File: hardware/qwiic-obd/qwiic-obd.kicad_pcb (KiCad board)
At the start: 4 copper layers, 109.9 x 52.7 mm, 157 parts, among them J101 I2C_STANDARD, J102 DB15_Female_HighDensity, J103 I2C_STANDARD, J401 1x4, J601 PIC-ICSPPOLAR_LOCK, Q201 2N7002, Q202 2N7002, Q203 2N7002, Q301 2N7002, Q501 DMG2301L, Q502 DMG2301L, Q503 MMBT3906, Q504 DMG2301L, Q601 DMG2301L, Q602 2N7002, Q603 2N7002, Q604 2N7002, Q605 2N7002, Q606 2N7002, Q607 2N7002, Q608 2N7002, Q609 2N7002, Q701 2N7002, Q702 2N7002, Q703 2N7002, Q704 MMBT3904, SW401 SW_Push, U201 TS5A3359DCUR, U202 TS5A3359DCUR, U203 TS5A3359DCUR, U204 TS5A3359DCUR, U205 TS5A3359DCUR, U301 TH8056KDC-AAA-008-RE, U302 MCP2557FD-xMF, U401 TCA9534, U402 MCP3423, U403 TCA9534, U404 ADM6320BX33ARJZ-R7, U501 AP63203WU, U502 XC9142B50CMR-G, U601 LM317L_SOT-89, U602 NCS20072, U603 PIC16F15225-I/ST, U701 NCS20072, U702 SC16IS741A, U801 SC18IS602BIPW_128, U802 MCP2515-xST, X701 ASV-12.000MHZ-EJ-T, X801 ASV-12.000MHZ-EJ-T

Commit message: And broke the ground plane again... fixed.
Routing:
- net J1850_BUS-: vias 11 -> 10
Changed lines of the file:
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@@
   (via (at 93.467701 41.651701) (size 0.8) (drill 0.4) (layers "F.Cu" "B.Cu") (net 12))
   (via (at 103.124 26.416) (size 0.8) (drill 0.4) (layers "F.Cu" "B.Cu") (net 12))
-  (via (at 88.9 24.892) (size 0.8) (drill 0.4) (layers "F.Cu" "B.Cu") (net 12))
   (via (at 69.596 42.672) (size 0.8) (drill 0.4) (layers "F.Cu" "B.Cu") (net 12))
   (via (at 81.788 43.688) (size 0.8) (drill 0.4) (layers "F.Cu" "B.Cu") (net 12))
@@
   (segment (start 88.9 24.892) (end 88.9 22.851402) (width 0.2) (layer "In2.Cu") (net 12))
   (segment (start 95.504 24.892) (end 94.996 24.892) (width 0.2) (layer "In2.Cu") (net 12))
+  (segment (start 94.996 24.892) (end 88.9 24.892) (width 0.2) (layer "In2.Cu") (net 12))
   (segment (start 91.952299 41.651701) (end 93.467701 41.651701) (width 0.2) (layer "In2.Cu") (net 12))
   (segment (start 105.156 28.956) (end 100.076 34.036) (width 0.2) (layer "In2.Cu") (net 12))
@@
   (segment (start 62.992 44.0182) (end 62.992 43.688) (width 0.2) (layer "B.Cu") (net 12))
   (segment (start 62.992 44.0182) (end 62.3062 44.0182) (width 0.2) (layer "B.Cu") (net 12))
-  (segment (start 94.996 24.892) (end 88.9 24.892) (width 0.2) (layer "B.Cu") (net 12))
   (segment (start 61.313 43.025) (end 56.870331 43.025) (width 0.2) (layer "B.Cu") (net 12))
   (segment (start 55.768984 49.895) (end 56.870331 49.895) (width 0.25) (layer "F.Cu") (net 13))

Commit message: Like I remember
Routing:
- net J1850_BUS-: track 88.2 -> 87.0 mm
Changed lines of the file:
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@@
   (segment (start 103.124 26.416) (end 97.028 26.416) (width 0.2) (layer "In2.Cu") (net 12))
   (segment (start 91.44 42.164) (end 91.952299 41.651701) (width 0.2) (layer "In2.Cu") (net 12))
-  (segment (start 88.9 24.892) (end 88.9 22.851402) (width 0.2) (layer "In2.Cu") (net 12))
+  (segment (start 90.932 24.892) (end 90.932 24.883402) (width 0.2) (layer "In2.Cu") (net 12))
+  (segment (start 94.996 24.892) (end 90.932 24.892) (width 0.2) (layer "In2.Cu") (net 12))
   (segment (start 95.504 24.892) (end 94.996 24.892) (width 0.2) (layer "In2.Cu") (net 12))
-  (segment (start 94.996 24.892) (end 88.9 24.892) (width 0.2) (layer "In2.Cu") (net 12))
   (segment (start 91.952299 41.651701) (end 93.467701 41.651701) (width 0.2) (layer "In2.Cu") (net 12))
   (segment (start 105.156 28.956) (end 100.076 34.036) (width 0.2) (layer "In2.Cu") (net 12))
-  (segment (start 88.9 22.851402) (end 87.888299 21.839701) (width 0.2) (layer "In2.Cu") (net 12))
+  (segment (start 90.932 24.883402) (end 87.888299 21.839701) (width 0.2) (layer "In2.Cu") (net 12))
   (segment (start 80.772 44.704) (end 81.788 43.688) (width 0.2) (layer "In2.Cu") (net 12))
   (segment (start 62.992 43.688) (end 64.008 42.672) (width 0.2) (layer "B.Cu") (net 12))

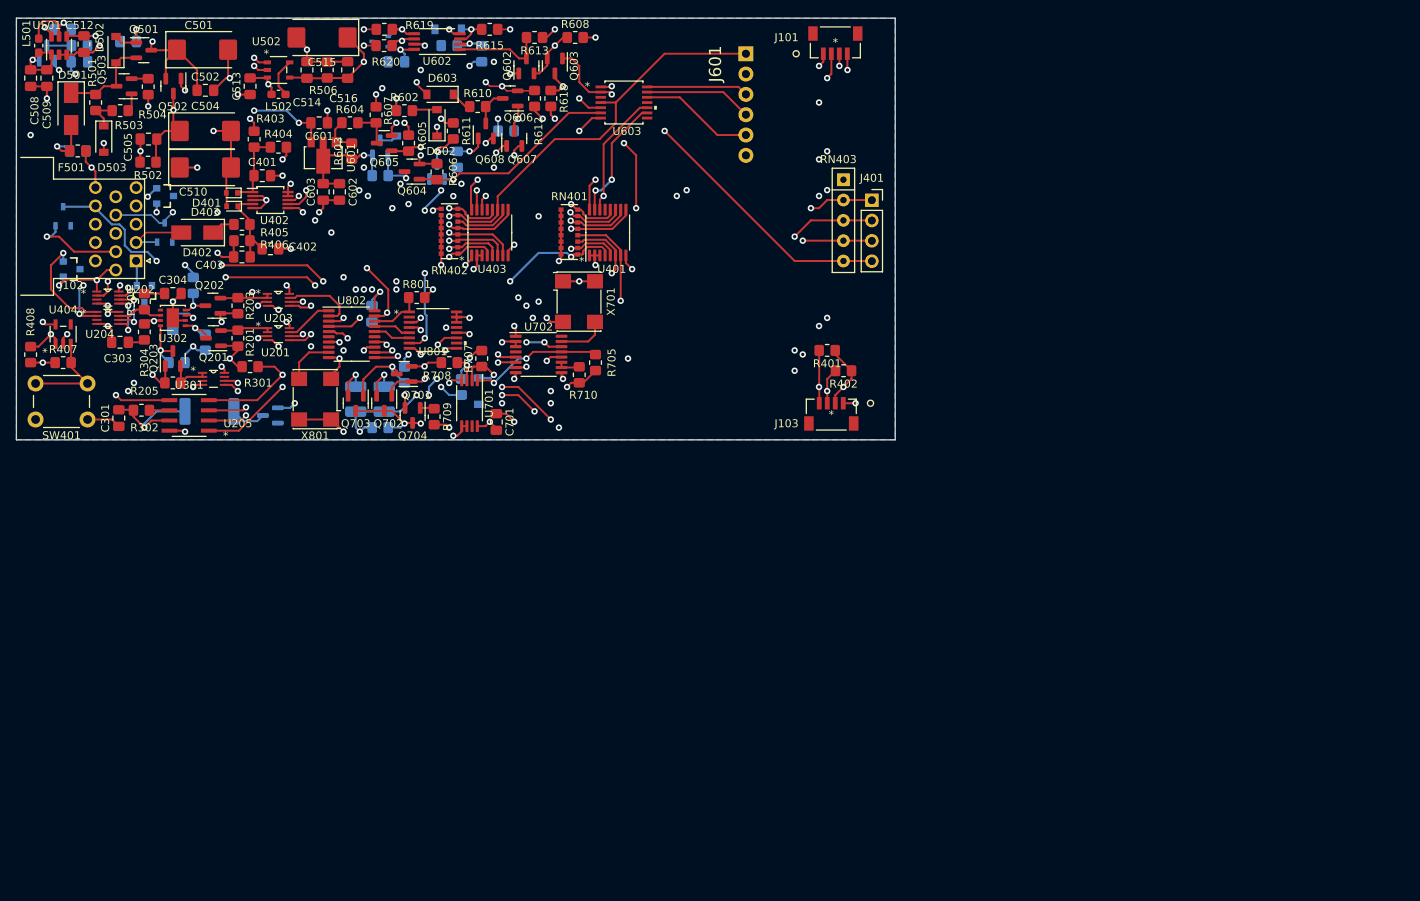
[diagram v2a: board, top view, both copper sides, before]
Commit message: Add PIC bootloader, update silkscreen
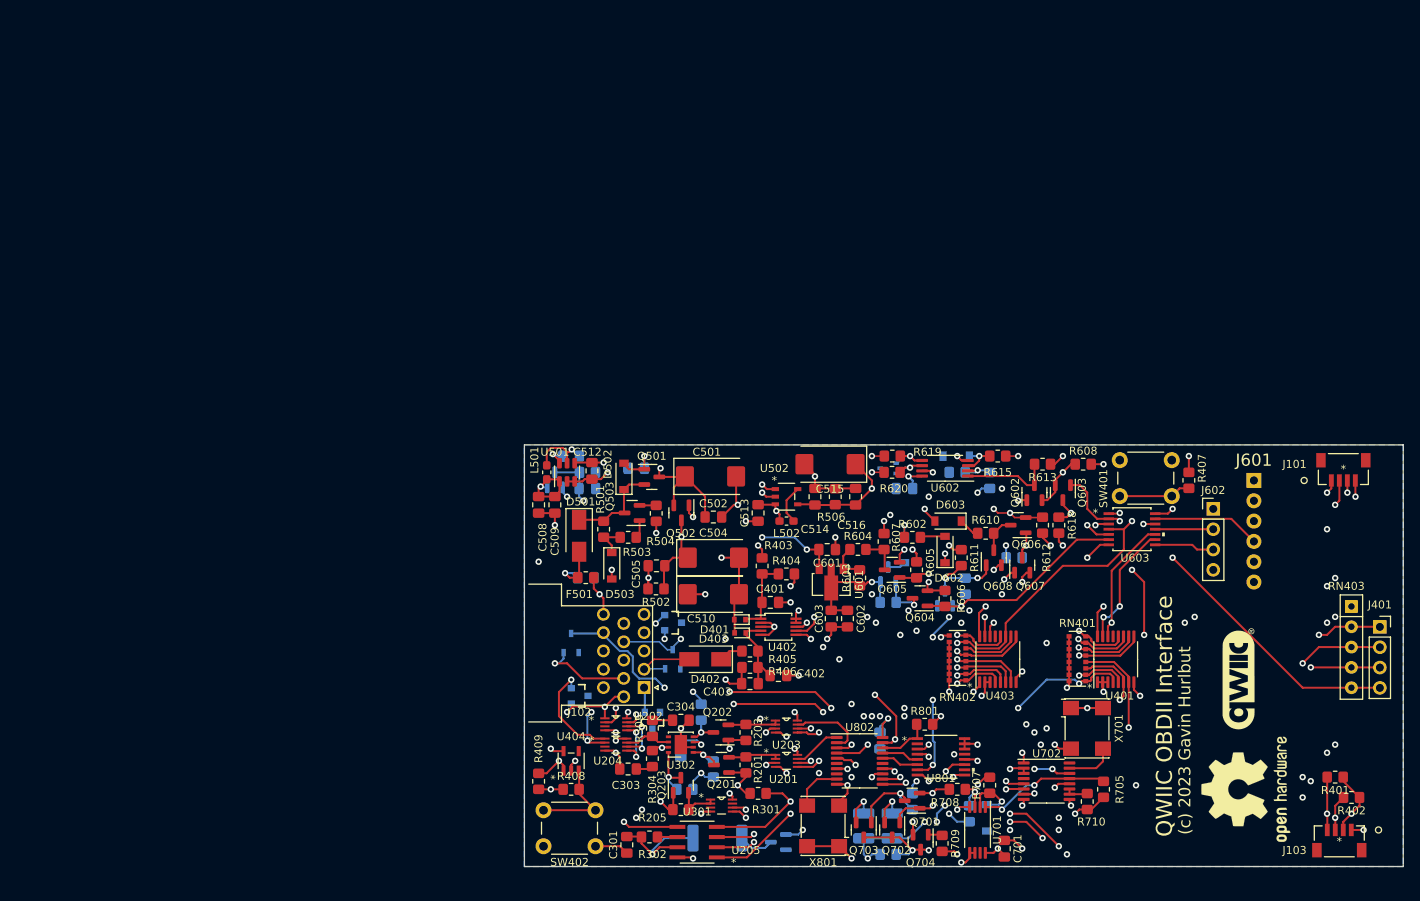
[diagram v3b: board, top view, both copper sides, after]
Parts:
- added G***: LOGO, local:qwiic-logo, F.Cu at (197.1, 101.1)
- added J602: PIC UART, Connector_PinHeader_2.54mm:PinHeader_1x04_P2.54mm_Vertical, F.Cu at (194.1, 79.8)
- added R407: 10k, Resistor_SMD:R_0805_2012Metric_Pad1.20x1.40mm_HandSolder, F.Cu at (191.0, 76.2)
- added REF**: OSHW-Logo2_14.6x12mm_SilkScreen, Symbol:OSHW-Logo2_14.6x12mm_SilkScreen, F.Cu at (198.1, 114.8)
- added SW401: SW_Push, Button_Switch_THT:SW_PUSH_6mm, F.Cu at (182.4, 73.7)
- J601: value PIC-ICSPPOLAR_LOCK -> PIC ICSP
- moved D401 82.9 mm to (134.9, 93.6)
- moved D402 82.9 mm to (130.6, 98.6)
- moved D601 82.9 mm to (155.4, 84.8)
- moved L502 82.9 mm to (140.7, 81.3)
- moved Q602 82.9 mm to (171.7, 77.7)
- moved R303 82.9 mm to (132.1, 120.9)
- moved R506 82.9 mm to (146.8, 78.2)
- moved R603 82.9 mm to (149.9, 88.4)
- moved R605 82.9 mm to (157.0, 87.4)
- moved R608 82.9 mm to (177.8, 74.2)
- moved R614 82.9 mm to (166.1, 76.2)
- moved R615 82.9 mm to (167.1, 73.2)
- moved R616 82.9 mm to (163.1, 89.4)
- moved R708 82.9 mm to (162.1, 114.8)
- moved RN401 82.9 mm to (177.1, 98.5)
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- renumbered R407 to R408, R408 to R409, SW401 to SW402
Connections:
- J601 pad 2: +3V3 -> +3V3_NOSW
- U603 pad 1: +3V3 -> +3V3_NOSW
- U603 pad 11: unconnected-(U603-Pad11) -> PIC_RX
- U603 pad 3: unconnected-(U603-Pad3) -> PIC_BL_ENTRY
- U603 pad 8: unconnected-(U603-Pad8) -> PIC_TX
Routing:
- net PIC_BL_ENTRY: track 0.00 -> 15.6 mm, vias 0 -> 1
- net GND: track 163.6 -> 153.3 mm, vias 54 -> 55
- net PIC_TX: track 0.00 -> 7.50 mm
- net PIC_RX: track 0.00 -> 7.26 mm
- net +3V3_NOSW: track 193.0 -> 196.5 mm, vias 9 -> 11
- net ICSPCLK: track 14.3 -> 17.2 mm, vias 0 -> 1
- net +3V3: track 75.5 -> 74.0 mm, vias 27 -> 26
- net ~{RESET}: vias 8 -> 9
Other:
- board text added: "(c) 2023 Gavin Hurlbut"
- board text added: "QWIIC OBDII Interface"

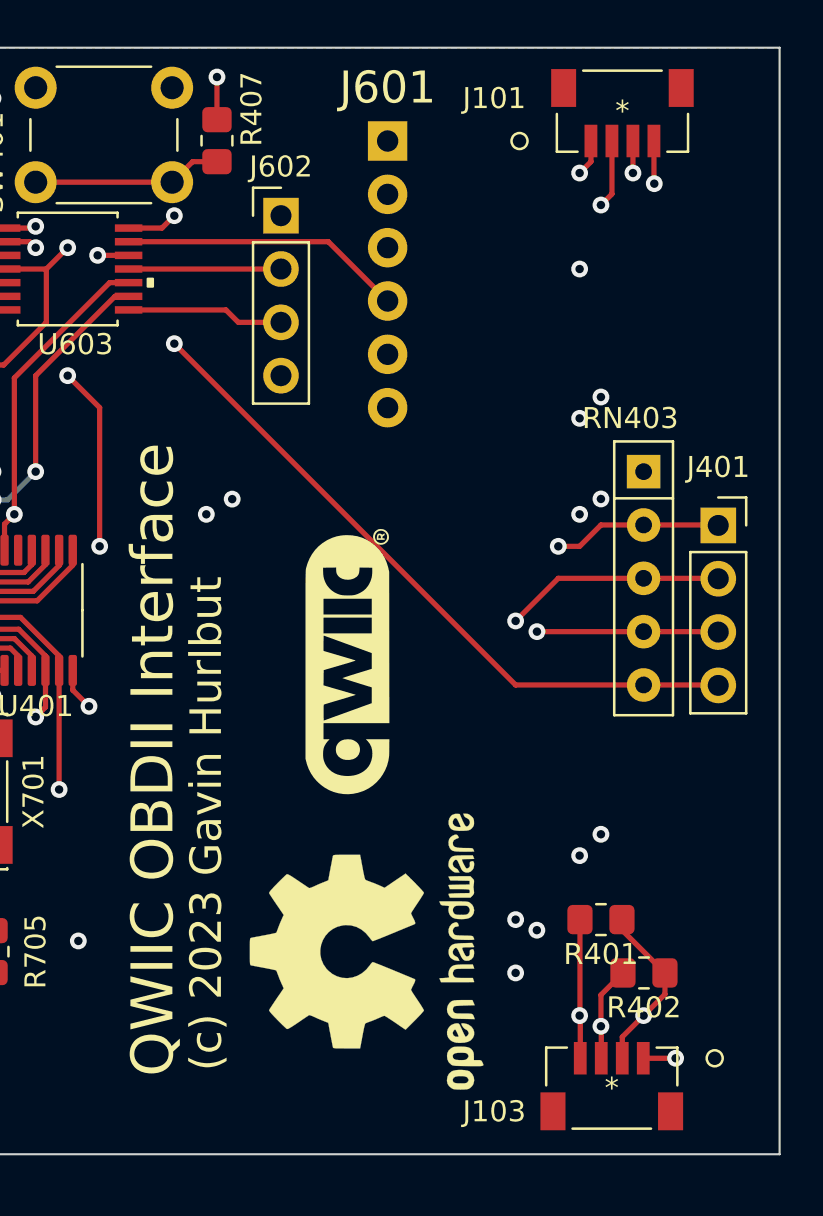
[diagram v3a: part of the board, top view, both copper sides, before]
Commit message: Added BL_LED on PA0, with a jumper
- if using ICSP, move jumper to 2,3 and PA0 is ISCPDAT
- if using bootloader, move jumper to 1,2 and PA0 is the LED
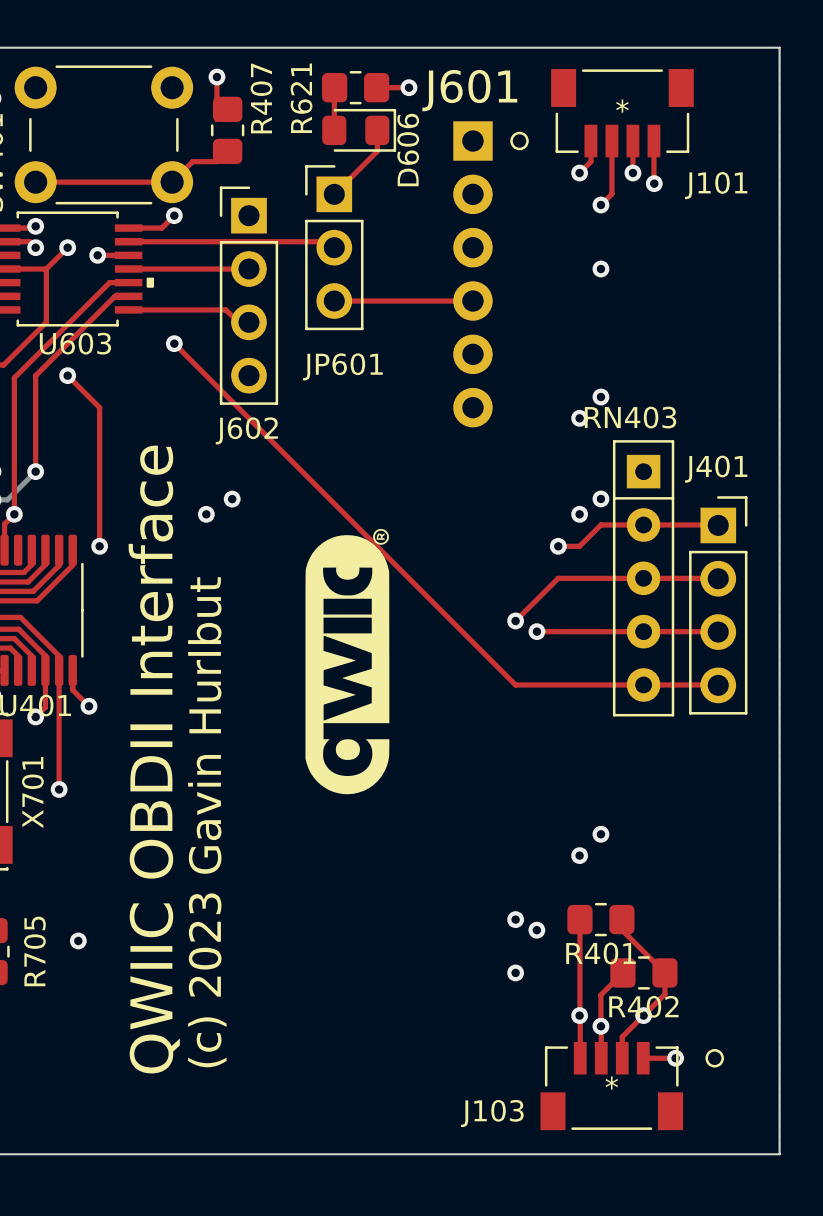
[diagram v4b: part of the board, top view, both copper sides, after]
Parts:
- removed REF**: OSHW-Logo2_14.6x12mm_SilkScreen, Symbol:OSHW-Logo2_14.6x12mm_SilkScreen
- added D606: LED, LED_SMD:LED_0805_2012Metric_Pad1.15x1.40mm_HandSolder, F.Cu at (197.6, 75.7)
- added JP601: BL_LED = 1,2 ICSP_DAT = 2,3, Connector_PinHeader_2.54mm:PinHeader_1x03_P2.54mm_Vertical, F.Cu at (196.6, 78.7)
- added R621: 330, Resistor_SMD:R_0805_2012Metric_Pad1.20x1.40mm_HandSolder, F.Cu at (197.6, 73.7)
- moved J601 4.06 mm to (203.2, 76.2)
- moved J602 1.52 mm to (192.5, 79.8)
- moved R407 0.71 mm to (191.5, 75.7)
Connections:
- net PIC_BL_ENTRY renamed ~{PIC_BL_ENTRY}
- U603 pad 13: ICSPDAT -> PA0
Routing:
- net PA0: track 0.00 -> 9.92 mm
- net ICSPDAT: track 13.5 -> 6.60 mm
- net ~{RESET}: track 145.3 -> 149.4 mm
- net ICSPCLK: track 17.2 -> 21.3 mm
- net ~{PIC_BL_LED}: track 0.00 -> 3.90 mm
- net Net-(D606-Pad2): track 0.00 -> 2.04 mm
- net +3V3_NOSW: track 196.5 -> 198.0 mm, vias 11 -> 12
- net PIC_TX: track 7.50 -> 5.98 mm
- net PIC_RX: track 7.26 -> 5.73 mm
- net SCL: track 168.3 -> 167.7 mm

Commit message: Added gerbers
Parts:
- added REF**: OSHW-Symbol_13.4x12mm_SilkScreen, Symbol:OSHW-Symbol_13.4x12mm_SilkScreen, F.Cu at (198.6, 114.3)
- moved G*** 3.41 mm to (198.6, 98.0)
- moved C512 1.31 mm to (115.8, 76.2)
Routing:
- net Net-(C507-Pad1): track 8.05 -> 10.9 mm
- net GND: track 153.3 -> 154.4 mm
- net ~{RESET}: track 149.4 -> 150.3 mm
- net +3V3_NOSW: track 198.0 -> 197.3 mm
- net +12V_NOSW: track 27.0 -> 27.7 mm
- net ICSPCLK: vias 1 -> 3
